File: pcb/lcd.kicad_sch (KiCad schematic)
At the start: 5 parts, among them J2 LCD, J4 LCD CTRL, J6 HC-05, U4 MC34063AD

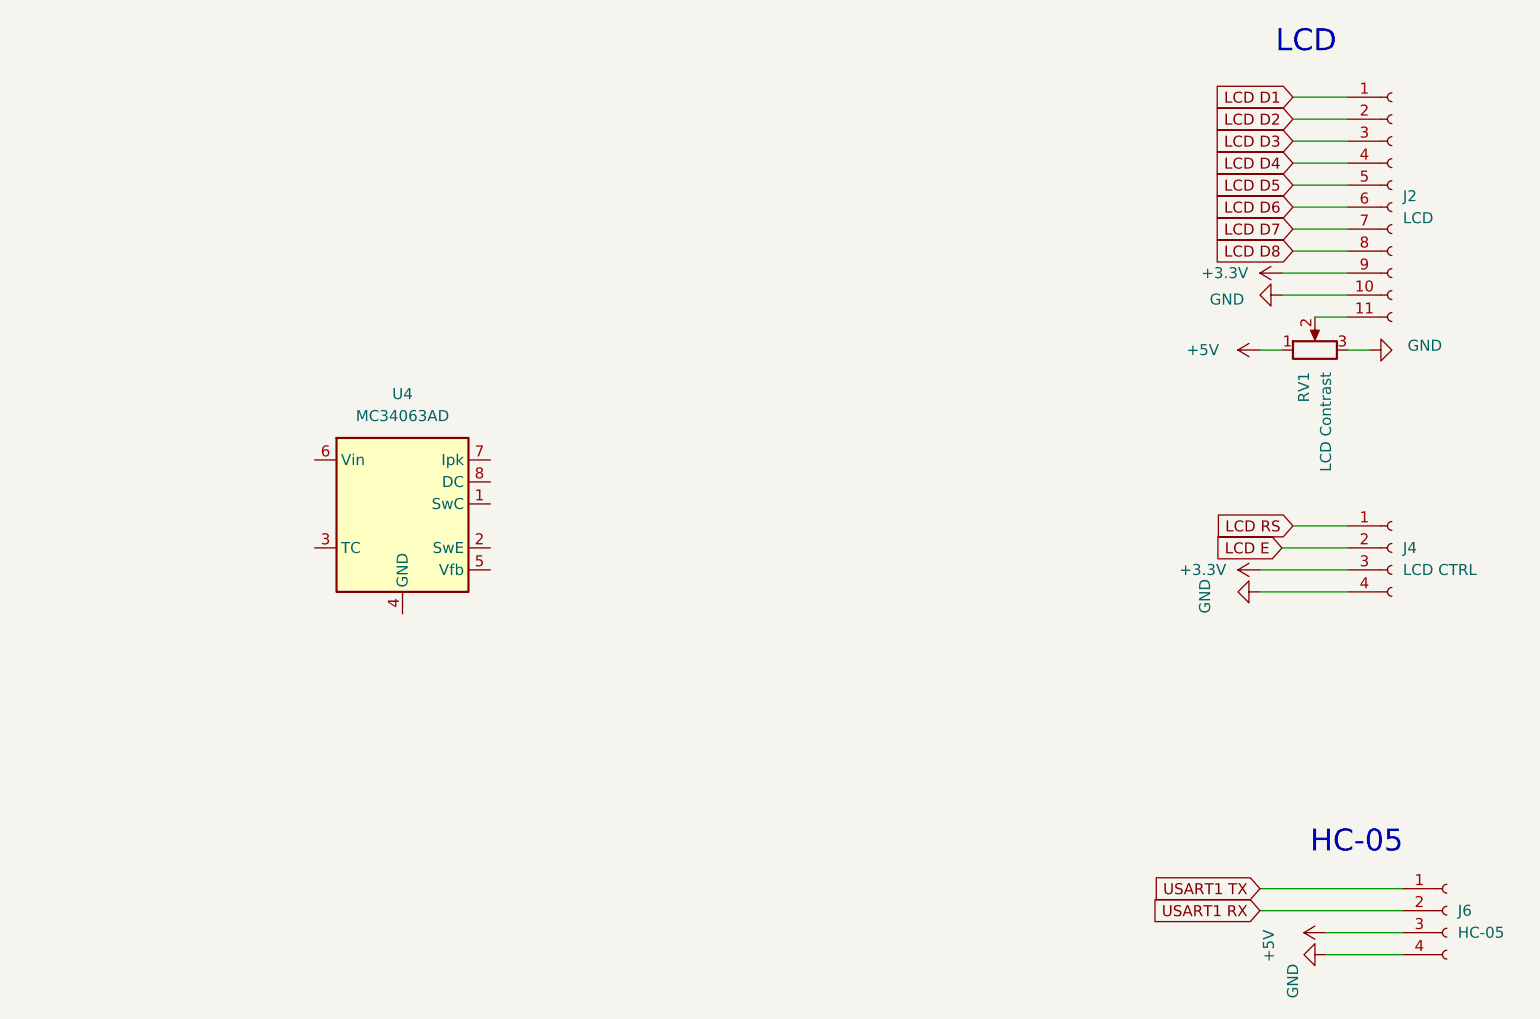
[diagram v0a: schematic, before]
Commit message: add boost converter to schematic
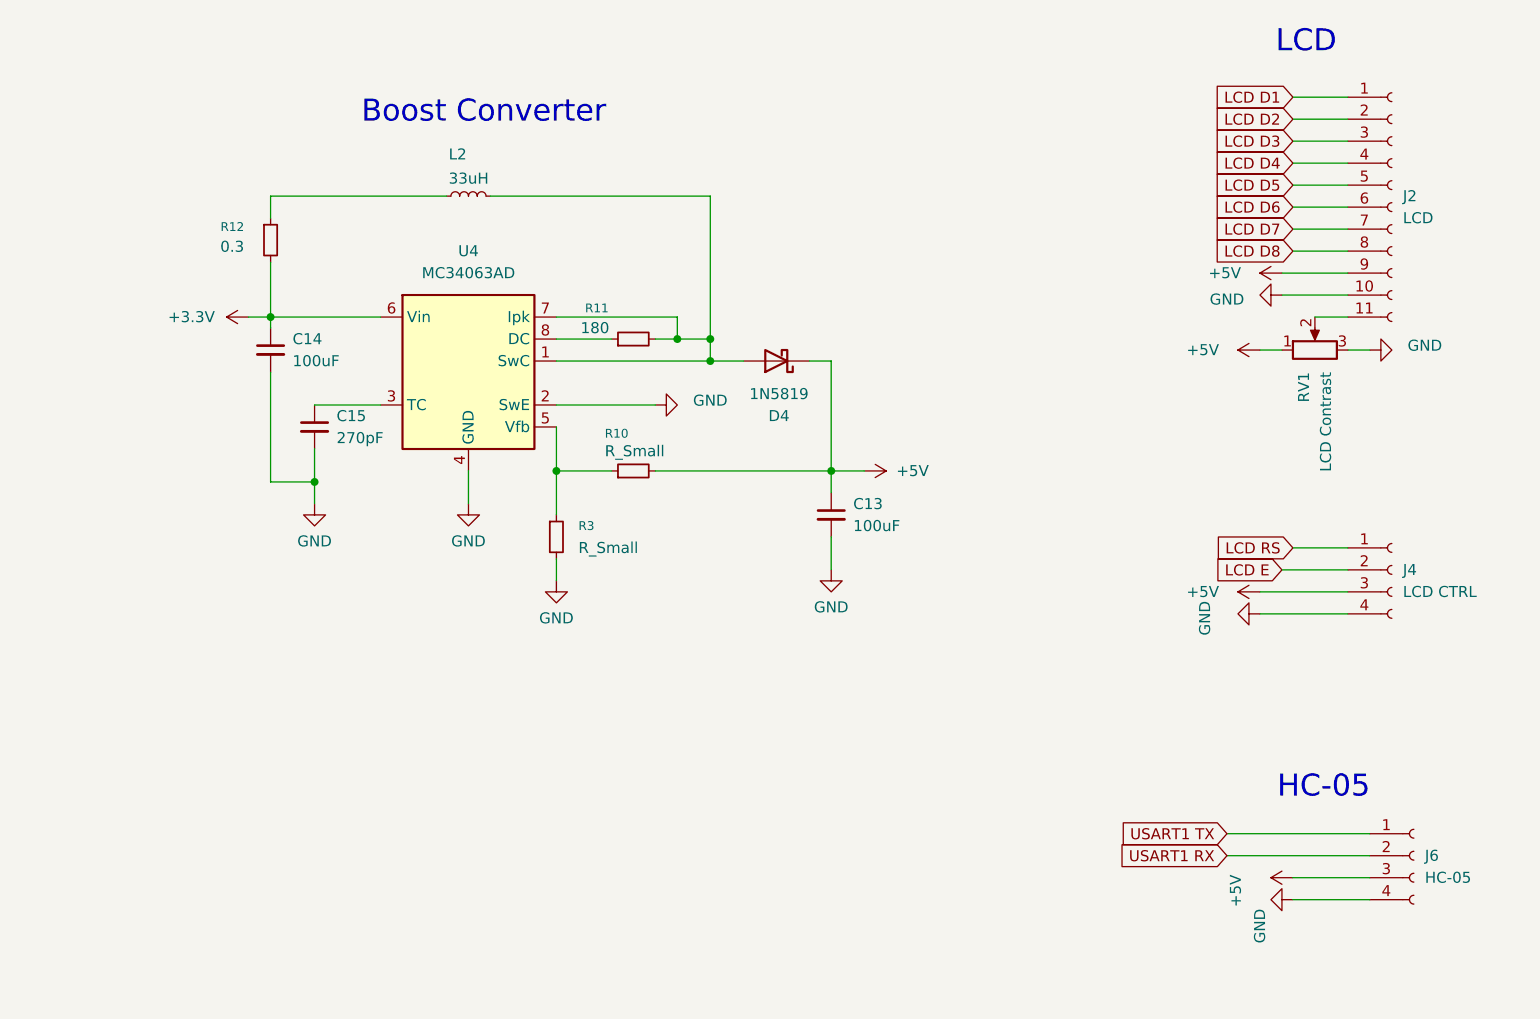
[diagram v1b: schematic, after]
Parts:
- added C13, C14: 100uF, symbol Device:C_Small
- added C15: 270pF, symbol Device:C_Small
- added D4: 1N5819, Diode_THT:D_DO-41_SOD81_P10.16mm_Horizontal, symbol Diode:1N5819
- added L2: 33uH, symbol Device:L_Small
- added R10, R3: R_Small, symbol Device:R_Small
- added R11: 180, symbol Device:R_Small
- added R12: 0.3, symbol Device:R_Small
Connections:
- net +3.3V: now also U4.6 (Vin), C14.1, R12.2; no longer J2.9 (Pin_9), J4.3 (Pin_3)
- net +5V: now also J2.9 (Pin_9), J4.3 (Pin_3), C13.1, D4.1 (K), R10.2
- net GND: now also U4.2 (SwE), U4.4 (GND), C13.2, C14.2, C15.2, R3.2
- net at U4.1 (SwC): now also U4.7 (Ipk), D4.2 (A), L2.2, R11.2
- net at U4.3 (TC): now also C15.1
- net at U4.5 (Vfb): now also R10.1, R3.1
- net at U4.8 (DC): now also R11.1
- new net: L2.1, R12.1
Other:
- note added: "Boost Converter"
- moved on the sheet: J4, J6, U4

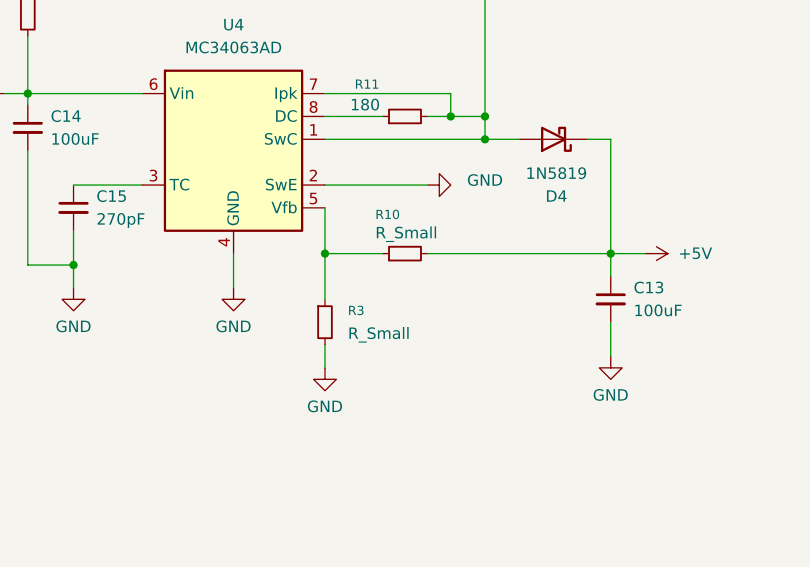
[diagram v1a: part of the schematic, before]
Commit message: add boost converter voltage divider
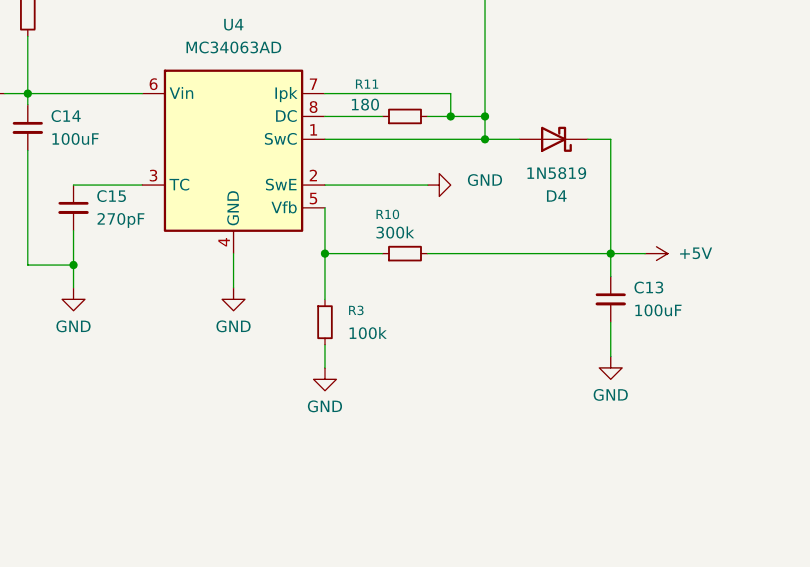
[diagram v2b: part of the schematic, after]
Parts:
- R10: value R_Small -> 300k
- R3: value R_Small -> 100k
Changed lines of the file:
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@@
 			)
 		)
-		(property "Value" "R_Small"
+		(property "Value" "100k"
 			(at 146.05 95.2499 0)
 			(effects
@@
 			)
 		)
-		(property "Value" "R_Small"
+		(property "Value" "300k"
 			(at 149.098 84.074 90)
 			(effects

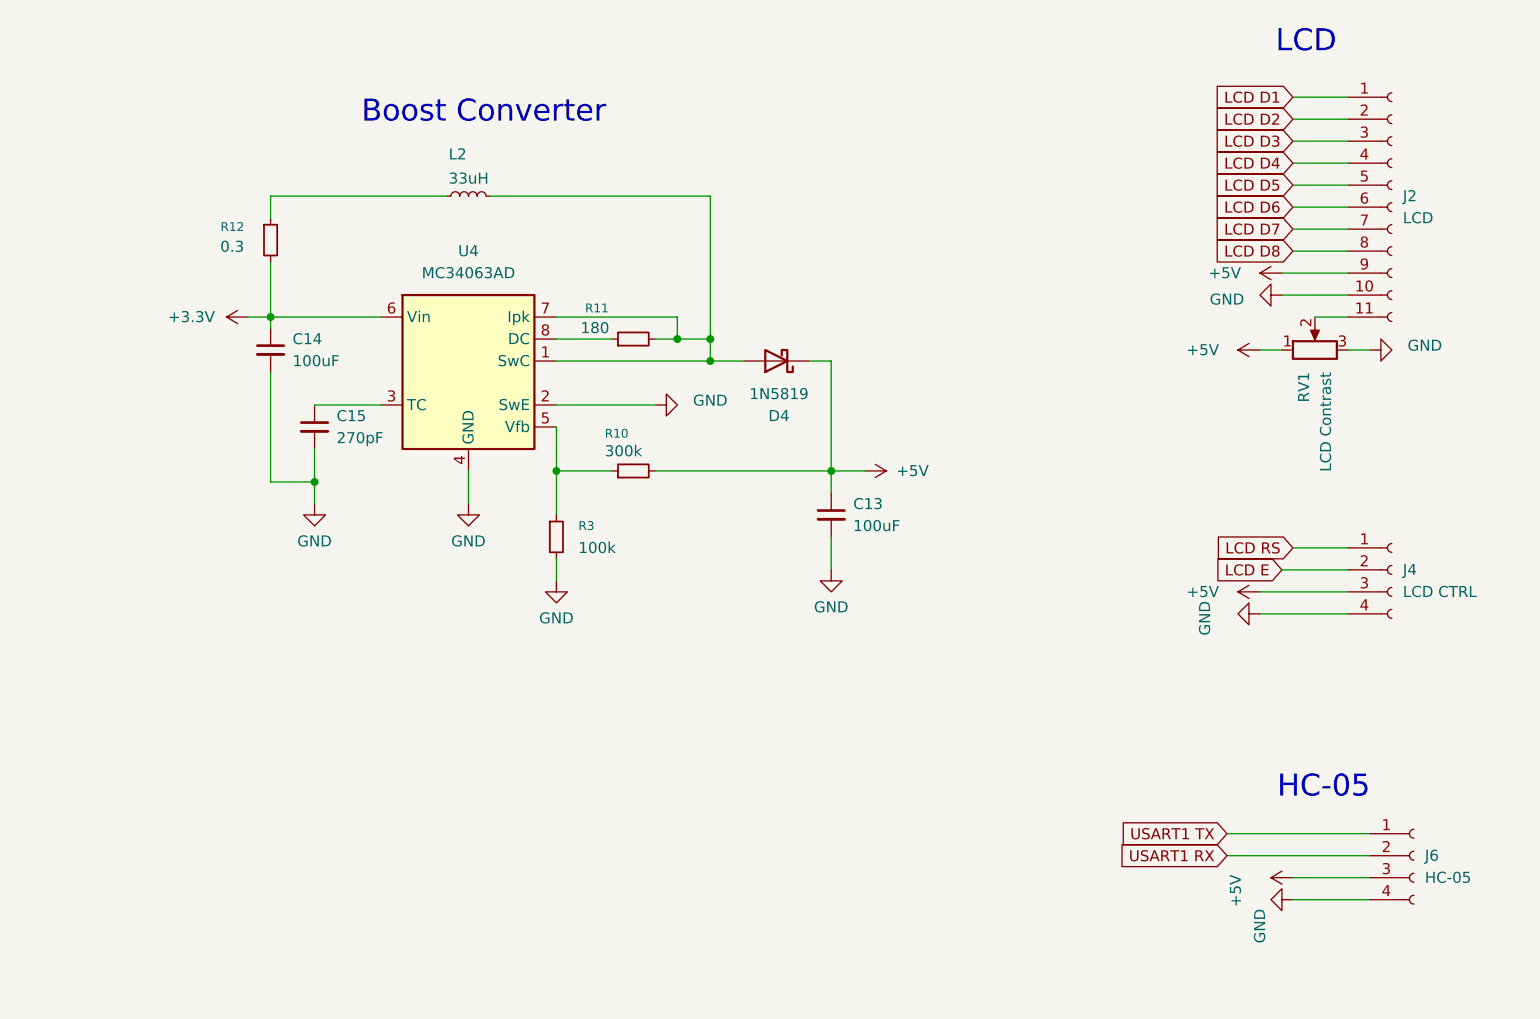
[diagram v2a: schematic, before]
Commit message: re-do boost converter
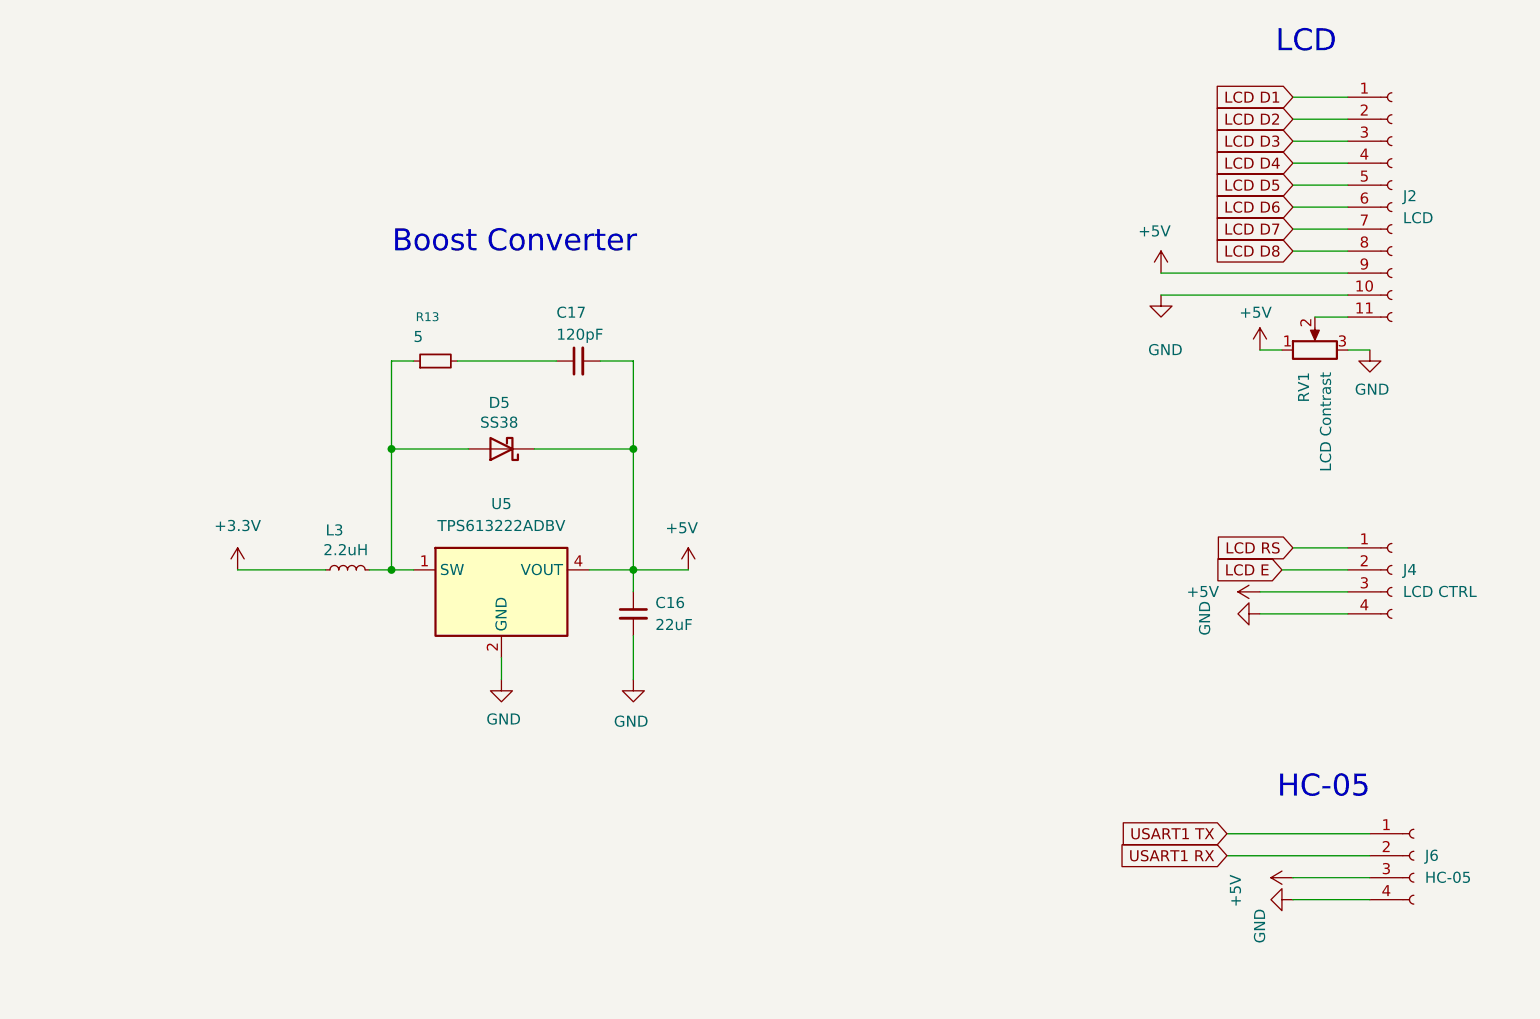
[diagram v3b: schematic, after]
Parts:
- removed C13, C14: 100uF, symbol Device:C_Small
- removed C15: 270pF, symbol Device:C_Small
- removed D4: 1N5819, Diode_THT:D_DO-41_SOD81_P10.16mm_Horizontal, symbol Diode:1N5819
- removed L2: 33uH, symbol Device:L_Small
- removed R10: 300k, symbol Device:R_Small
- removed R11: 180, symbol Device:R_Small
- removed R12: 0.3, symbol Device:R_Small
- removed R3: 100k, symbol Device:R_Small
- removed U4: MC34063AD, Package_SO:SOIC-8_3.9x4.9mm_P1.27mm, symbol Regulator_Switching:MC34063AD
- added C16: 22uF, symbol Device:C_Small
- added C17: 120pF, Capacitor_SMD:C_0603_1608Metric_Pad1.08x0.95mm_HandSolder, symbol Device:C_Small
- added D5: SS38, Diode_SMD:D_SMA, symbol Diode:SS38
- added L3: 2.2uH, symbol Device:L_Small
- added R13: 5, Resistor_SMD:R_0201_0603Metric_Pad0.64x0.40mm_HandSolder, symbol Device:R_Small
- added U5: TPS613222ADBV, Package_TO_SOT_SMD:SOT-23-5, symbol Regulator_Switching:TPS613222ADBV
- RV1: footprint Potentiometer_SMD:Potentiometer_Bourns_3224W_Vertical -> Potentiometer_SMD:Potentiometer_Bourns_TC33X_Vertical
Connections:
- net +3.3V: now also L3.1
- net +5V: now also C16.1, C17.2, D5.1 (K), U5.4 (VOUT)
- net GND: now also C16.2, U5.2 (GND)
- new net: D5.2 (A), L3.2, R13.1, U5.1 (SW)
- new net: C17.1, R13.2

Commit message: add footprints and update parts list
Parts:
- C16: footprint (none) -> Capacitor_SMD:C_0603_1608Metric_Pad1.08x0.95mm_HandSolder
- C17: value 120pF -> 1nF
- J2: footprint (none) -> Connector_PinHeader_2.54mm:PinHeader_1x11_P2.54mm_Vertical
- L3: footprint (none) -> Inductor_SMD:L_0603_1608Metric_Pad1.05x0.95mm_HandSolder
- R13: value 5 -> 10
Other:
- note added: "Datasheet gives typical values of R13 and C17 as 5 ohms and 120pF however these were hard to find in 0603 package"
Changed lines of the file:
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@@
+		)
+	)
+	(text "Datasheet gives typical values of R13 and C17 \nas 5 ohms and 120pF however these were \nhard to find in 0603 package"
+		(exclude_from_sim no)
+		(at 103.124 69.342 0)
+		(effects
+			(font
+				(size 1.016 1.016)
+			)
 		)
 	)
@@
 			)
 		)
-		(property "Value" "5"
+		(property "Value" "10"
 			(at 127 70.866 90)
 			(effects
@@
 			)
 		)
-		(property "Footprint" ""
+		(property "Footprint" "Inductor_SMD:L_0603_1608Metric_Pad1.05x0.95mm_HandSolder"
 			(at 119.38 97.79 0)
 			(effects
@@
 			)
 		)
-		(property "Footprint" ""
+		(property "Footprint" "Connector_PinHeader_2.54mm:PinHeader_1x11_P2.54mm_Vertical"
 			(at 240.03 55.88 0)
 			(effects
@@
 			)
 		)
-		(property "Footprint" ""
+		(property "Footprint" "Capacitor_SMD:C_0603_1608Metric_Pad1.08x0.95mm_HandSolder"
 			(at 152.4 102.87 0)
 			(effects
@@
 			)
 		)
-		(property "Value" "120pF"
+		(property "Value" "1nF"
 			(at 143.51 70.612 90)
 			(effects

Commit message: start re-designing pcb
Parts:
- R13: footprint Resistor_SMD:R_0201_0603Metric_Pad0.64x0.40mm_HandSolder -> Resistor_SMD:R_0603_1608Metric_Pad0.98x0.95mm_HandSolder
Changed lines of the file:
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@@
 			)
 		)
-		(property "Footprint" "Resistor_SMD:R_0201_0603Metric_Pad0.64x0.40mm_HandSolder"
+		(property "Footprint" "Resistor_SMD:R_0603_1608Metric_Pad0.98x0.95mm_HandSolder"
 			(at 129.54 73.66 0)
 			(effects
